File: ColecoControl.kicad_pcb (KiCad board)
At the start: 2 copper layers, 99.1 x 49.9 mm, 50 parts, among them J1 Conn_01x39, J3 DB9_Male, J4 DB9_Male, SW1 1, SW10 0, SW11 *, SW12 #, SW2 2, SW3 3, SW4 4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

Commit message: Finishing touches
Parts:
- added J2: BTN/CTRL, Connector_PinHeader_2.54mm:PinHeader_1x03_P2.54mm_Vertical, F.Cu at (233.7, 122.8)
- U2: value 74LS138 -> 74HCT138
- U6: value 74LS258 -> 74HCT258
- moved C2 3.15 mm to (236.8, 122.8), turned to 270 degrees
- moved D1 2.57 mm to (204.4, 129.3)
- moved D11 2.57 mm to (174.0, 131.9)
- moved D15 2.57 mm to (174.0, 134.4)
- moved D16 2.57 mm to (174.0, 121.7)
- moved D17 2.57 mm to (174.0, 129.3)
- moved D18 2.57 mm to (174.0, 124.2)
- moved D19 2.57 mm to (204.4, 121.7)
- moved D21 2.57 mm to (204.4, 124.2)
- moved D3 2.57 mm to (204.4, 126.8)
- moved D4 2.57 mm to (174.0, 126.8)
- moved D6 2.57 mm to (204.4, 131.9)
- moved D10 2.57 mm to (194.3, 121.7)
- moved D12 2.57 mm to (194.3, 131.9)
- moved D13 2.57 mm to (194.3, 126.8)
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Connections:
- net /CTRL_R renamed /~CTRL_R~
- U2 pad 11: /CTRL_EN_1 -> /~CTRL_EN_1~
- U2 pad 15: /CTRL_EN_2 -> /~CTRL_EN_2~
- U2 pad 4: Net-(U2-Pad4) -> /M1
- U3 pad 1: /CTRL_EN_1 -> /~M1~
- U3 pad 10: /A1 -> /~CTRL_EN_1~
- U3 pad 11: Net-(U2-Pad4) -> /~SELECT~
- U3 pad 12: /~M1~ -> /~CTRL_EN_2~
- U3 pad 13: /~M1~ -> /SELECT
- U3 pad 2: /SELECT -> /~M1~
- U3 pad 3: Net-(U3-Pad3) -> /M1
- U3 pad 4: Net-(U3-Pad3) -> /A1
- U3 pad 5: /CTRL_EN_2 -> /A1
- U3 pad 6: /SELECT -> /~A1~
- U3 pad 8: Net-(U3-Pad8) -> /SELECT
- U3 pad 9: /A1 -> /~SELECT~
- U4 pad 19: Net-(U3-Pad8) -> /~A1~
- U6 pad 1: /SELECT -> Net-(J2-Pad2)
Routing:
- net /~A1~: track 0.00 -> 41.2 mm
- net /CTRL_EN_2: track 38.4 -> 0.00 mm, vias 1 -> 0
- net Net-(U3-Pad8): track 35.2 -> 0.00 mm
- net /~CTRL_EN_2~: track 0.00 -> 28.8 mm, vias 0 -> 1
- net Net-(U2-Pad4): track 27.4 -> 0.00 mm
- net /~CTRL_EN_1~: track 0.00 -> 24.8 mm, vias 0 -> 1
- net /M1: track 0.00 -> 23.5 mm
- net /SELECT: track 153.8 -> 130.9 mm
- net /CTRL_EN_1: track 19.2 -> 0.00 mm, vias 1 -> 0
- net VCC: track 151.5 -> 163.7 mm
- net /~MUX1L~: track 58.3 -> 46.1 mm, vias 0 -> 1
- net /~M1~: track 14.0 -> 6.37 mm
- net Net-(D19-Pad1): track 27.3 -> 34.4 mm, vias 1 -> 0
- net /~FIRE2~: track 72.1 -> 65.9 mm, vias 1 -> 0
- net /~SELECT~: track 0.00 -> 6.01 mm
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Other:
- board text added: "Coleco Controller Interface REV1 https://github.com/jblang/ColecoController (c) 2018 J.B. Langston"
- board text removed: "https://github.com/jblang/colecoctrl (c) 2018 J.B. Langston"

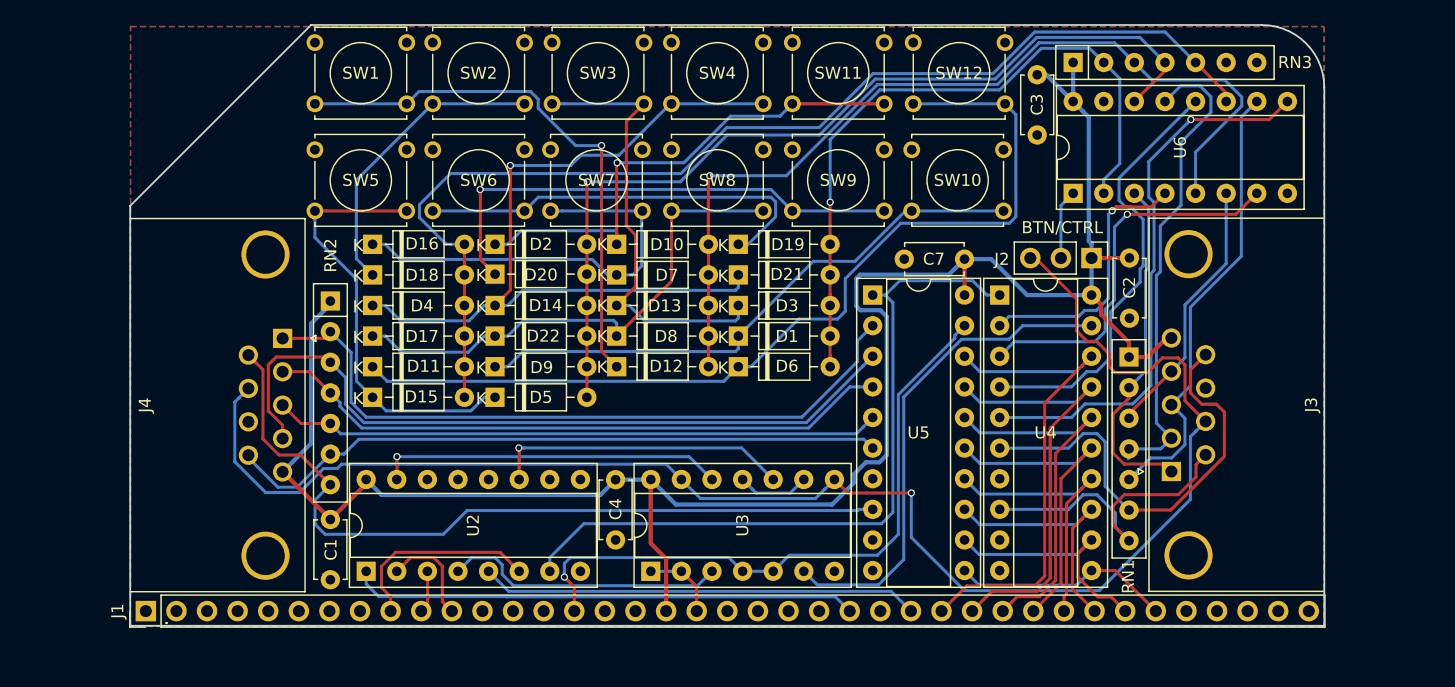
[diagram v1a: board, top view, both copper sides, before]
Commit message: Add jumper to support real ColecoVision controllers
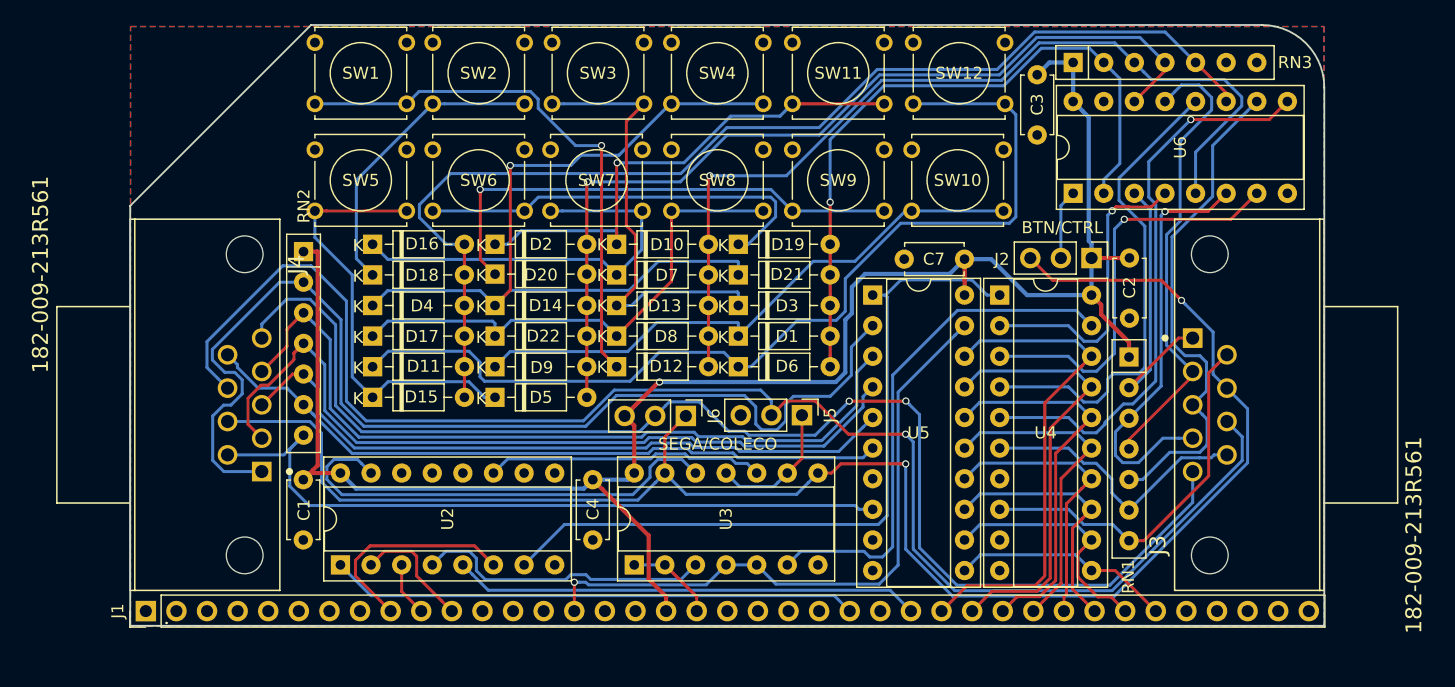
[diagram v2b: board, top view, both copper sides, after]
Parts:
- added J5: SEGA/COLECO, Connector_PinHeader_2.54mm:PinHeader_1x03_P2.54mm_Vertical, F.Cu at (209.7, 135.9)
- added J6: SEGA/COLECO, Connector_PinHeader_2.54mm:PinHeader_1x03_P2.54mm_Vertical, F.Cu at (200.0, 136.0)
- J3, J4: value DB9_Male -> 182-009-213R561; footprint Connector_Dsub:DSUB-9_Male_Horizontal_P2.77x2.84mm_EdgePinOffset9.90mm_Housed_MountingHolesOffset11.32mm -> 182-009-213R561:NORCOMP_182-009-213R561
- moved J3 6.39 mm to (243.5, 135.0)
- moved J4 6.35 mm to (163.4, 135.0)
- moved RN2 4.67 mm to (168.3, 122.3)
- moved C1 3.99 mm to (168.3, 141.2)
- moved U2 2.20 mm to (171.3, 148.3)
- moved C4 1.89 mm to (192.3, 141.2)
- moved U3 1.47 mm to (195.7, 148.3)
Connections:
- J3 pad 5: VCC -> Net-(J3-Pad5)
- J3 pad 8: GND -> Net-(J3-Pad8)
- J4 pad 5: VCC -> Net-(J3-Pad5)
- J4 pad 8: GND -> Net-(J3-Pad8)
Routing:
- net Net-(J3-Pad8): track 0.00 -> 126.4 mm, vias 0 -> 1
- net Net-(J3-Pad5): track 0.00 -> 109.3 mm, vias 0 -> 2
- net /~UP2~: track 58.7 -> 91.5 mm
- net /~DOWN2~: track 52.5 -> 66.5 mm
- net /~RIGHT1~: track 22.0 -> 35.1 mm, vias 0 -> 1
- net /~ALT1~: track 36.6 -> 23.6 mm
- net VCC: track 163.7 -> 152.6 mm, vias 0 -> 1
- net /SELECT: track 130.9 -> 140.9 mm, vias 1 -> 2
- net /~CTRL_EN_2~: track 28.8 -> 38.7 mm, vias 1 -> 0
- net /~LEFT2~: track 50.5 -> 57.1 mm
- net /~SELECT~: track 6.01 -> 11.3 mm
- net /~FIRE2~: track 65.9 -> 60.9 mm
- net /~FIRE1~: track 27.0 -> 31.3 mm
- net /~LEFT1~: track 37.7 -> 42.0 mm
- net /~UP1~: track 28.8 -> 24.6 mm
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
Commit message: Updates for REV2
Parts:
- J3: value 182-009-213R561 -> PLAYER 1; footprint 182-009-213R561:NORCOMP_182-009-213R561 -> 182-009-213R561:NORCOMP_182-009-113R561
- J4: value 182-009-213R561 -> PLAYER 2; footprint 182-009-213R561:NORCOMP_182-009-213R561 -> 182-009-213R561:NORCOMP_182-009-113R561
- moved J4 0.08 mm to (163.4, 135.0)
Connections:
- U4 pad 19: /~A1~ -> /A1
- U4 pad 7: GND -> VCC
- U5 pad 19: /A1 -> /~A1~
- U5 pad 7: GND -> VCC
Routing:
- net VCC: track 152.6 -> 189.5 mm, vias 1 -> 0
- net /~FIRE2~: track 60.9 -> 85.3 mm
- net /~UP2~: track 91.5 -> 69.0 mm
- net Net-(J3-Pad5): track 109.3 -> 131.4 mm, vias 2 -> 1
- net /~RIGHT2~: track 66.1 -> 79.8 mm
- net Net-(J3-Pad8): track 126.4 -> 113.9 mm
- net /~RIGHT1~: track 35.1 -> 24.1 mm, vias 1 -> 0
- net /~UP1~: track 24.6 -> 35.4 mm
- net /~A1~: track 43.3 -> 32.7 mm
- net /~ALT1~: track 23.6 -> 33.8 mm
- net /A1: track 53.5 -> 63.6 mm
- net /~CTRL_EN_2~: track 38.7 -> 30.4 mm, vias 0 -> 1
- net /~DOWN2~: track 66.5 -> 58.4 mm
- net /~SELECT~: track 11.3 -> 17.9 mm
- net /~FIRE1~: track 31.3 -> 26.9 mm
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
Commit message: Update revision number on board
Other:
- board text added: "Coleco Controller Interface REV2 https://github.com/jblang/ColecoController (c) 2018 J.B. Langston"
- board text removed: "Coleco Controller Interface REV1 https://github.com/jblang/ColecoController (c) 2018 J.B. Langston"
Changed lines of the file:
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@@
       (net 58 "Net-(J3-Pad5)"))
   )
-  (gr_text "Coleco Controller Interface REV1\n\nhttps://github.com/jblang/ColecoController\n(c) 2018 J.B. Langston" (at 190.2841 141.9352) (layer B.SilkS)
+  (gr_text "Coleco Controller Interface REV2\n\nhttps://github.com/jblang/ColecoController\n(c) 2018 J.B. Langston" (at 190.2841 141.9352) (layer B.SilkS)
     (effects (font (size 1.25 1.25) (thickness 0.3)) (justify mirror))
   )
